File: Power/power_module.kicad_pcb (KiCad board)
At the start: 4 copper layers, 183 x 90 mm, 53 parts, among them J1 Conn_02x03_Odd_Even, J2 Conn_02x03_Odd_Even, J3 Conn_02x06_Counter_Clockwise, J4 Conn_02x05_Top_Bottom, J5 Conn_02x05_Top_Bottom, J6 Conn_02x02_Odd_Even, J7 Conn_02x02_Odd_Even, P3 CONN_01X04, P6 CONN_01X04, Q1 Q_NMOS_GDS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

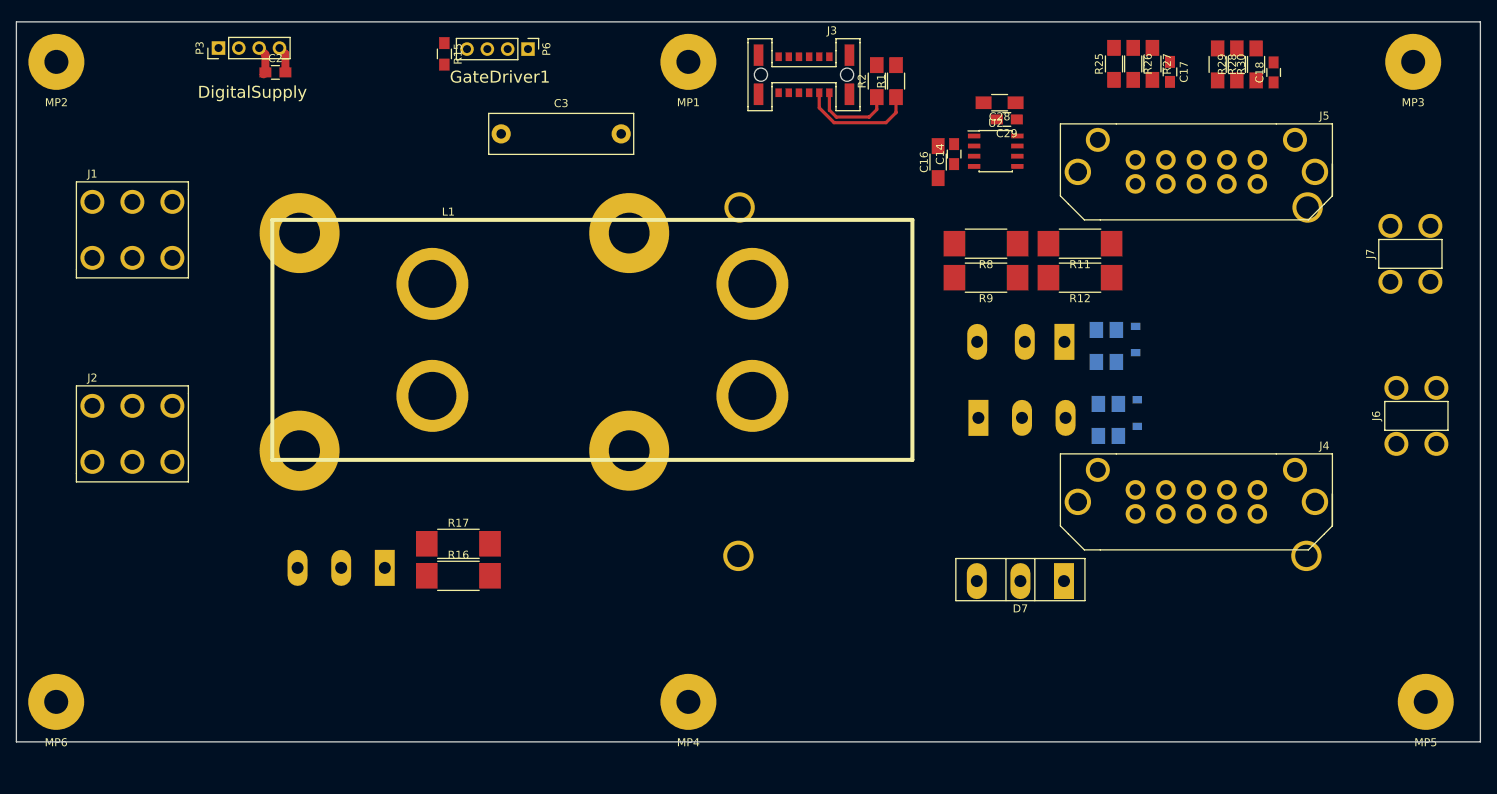
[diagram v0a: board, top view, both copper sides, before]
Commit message: Mevcut yerlesime gore kaba cizim yapildi.
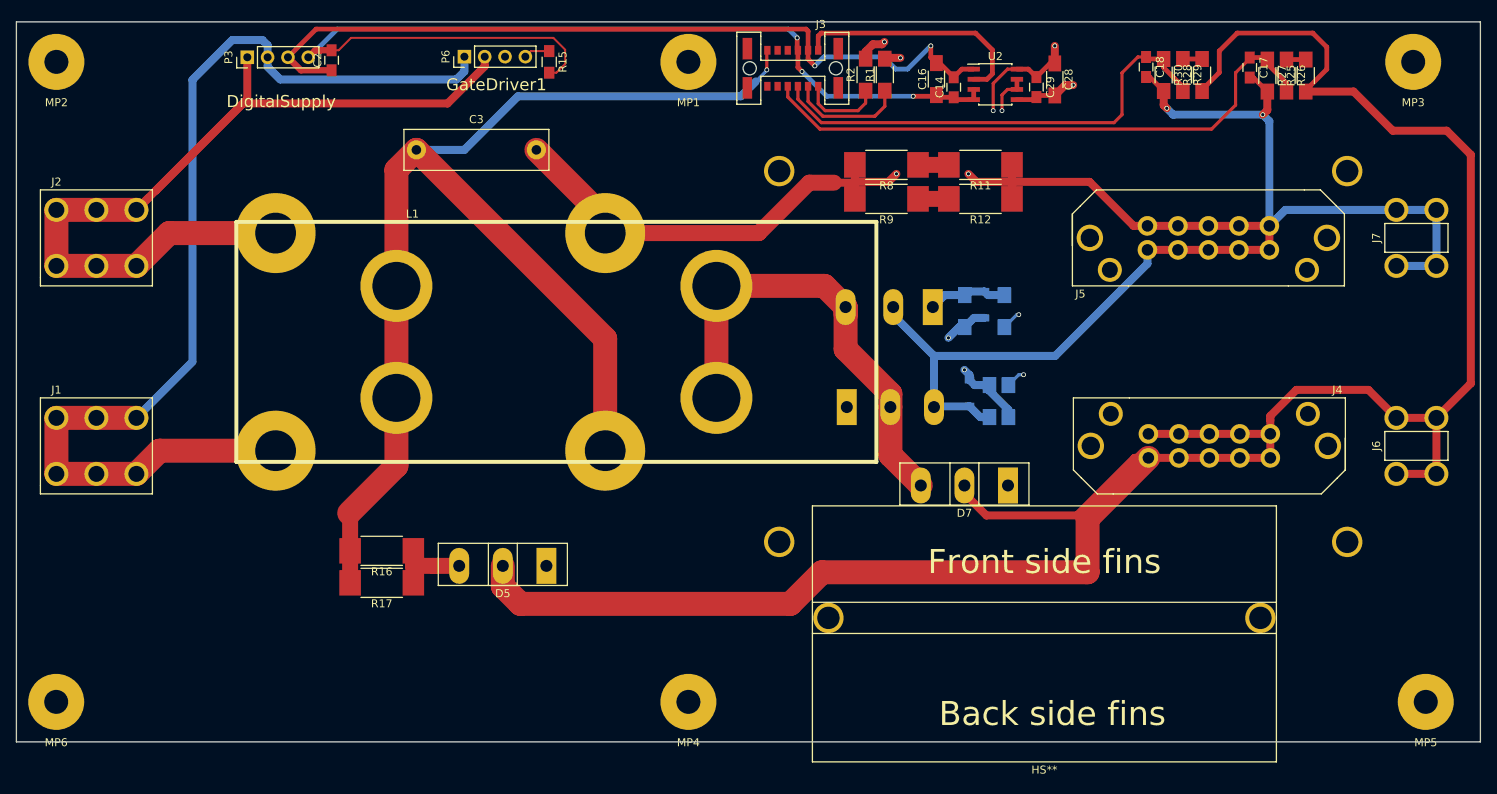
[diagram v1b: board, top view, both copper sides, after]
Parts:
- added HS**: HS_OhmiteC40, NamchoLibs:HS_OhmiteC40, F.Cu at (185.5, 149.5)
- D5: moved to F.Cu
- moved J1 27.4 mm to (67.0, 128.0)
- moved J2 24.9 mm to (67.0, 102.0)
- moved R25 24.0 mm to (218.2, 81.7)
- moved D3 21.1 mm to (176.1, 121.4), turned to 270 degrees
- moved D5 20.2 mm to (123.2, 143.0)
- moved D2 19.4 mm to (178.0, 110.3)
- moved R26 19.2 mm to (215.8, 81.7)
- moved Q1 17.0 mm to (171.6, 110.7)
- moved R31 17.0 mm to (175.6, 111.2)
- moved Q2 16.5 mm to (160.8, 123.2)
- moved R32 16.3 mm to (178.6, 122.4), turned to 90 degrees
- moved C18 16.0 mm to (198.2, 80.6), turned to 270 degrees
- moved R11 15.9 mm to (177.5, 92.9)
- moved R12 15.9 mm to (177.5, 97.1)
- moved R8 15.9 mm to (165.8, 92.9)
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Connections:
- D5 pad 2: Net-(D5-Pad2) -> /Vout+
- P6 pad 1: /PH2 -> /PH1
- P6 pad 2: /PH1 -> /PH2
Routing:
- net GNDA: track 0.15 -> 350.8 mm, vias 0 -> 7
- net /Vout+: track 0.00 -> 281.3 mm
- net Vin_Sens: track 0.00 -> 160.9 mm, vias 0 -> 1
- net /PH1: track 0.00 -> 132.7 mm
- net GNDD: track 3.46 -> 129.8 mm, vias 0 -> 3
- net /PH2: track 0.00 -> 121.8 mm
- net VDD: track 3.71 -> 102.5 mm, vias 0 -> 2
- net /15V/1: track 0.00 -> 88.7 mm, vias 0 -> 1
- net /Bridge-: track 0.00 -> 80.0 mm, vias 0 -> 2
- net Vout: track 0.00 -> 74.2 mm
- net Vop: track 0.00 -> 60.1 mm
- net /CrtPad: track 0.00 -> 58.4 mm
- net Net-(R14-Pad2): track 0.00 -> 44.4 mm, vias 0 -> 3
- net Gate_Drv: track 0.00 -> 30.2 mm
- net Net-(D3-Pad1): track 0.00 -> 26.5 mm, vias 0 -> 1
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
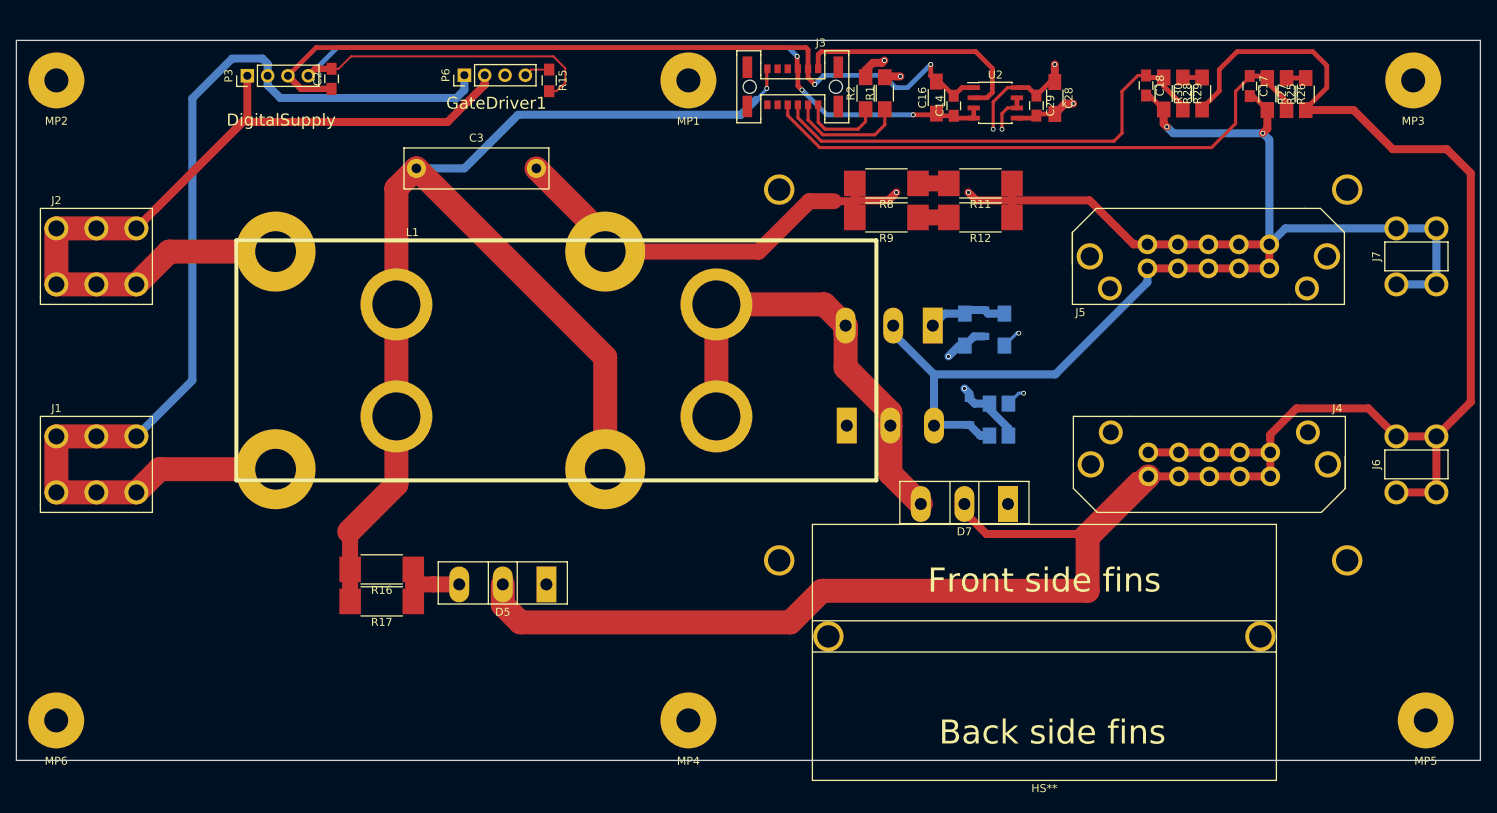
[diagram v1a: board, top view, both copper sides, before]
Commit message: Guc akisindaki hat/poligonlar tamamlandi.
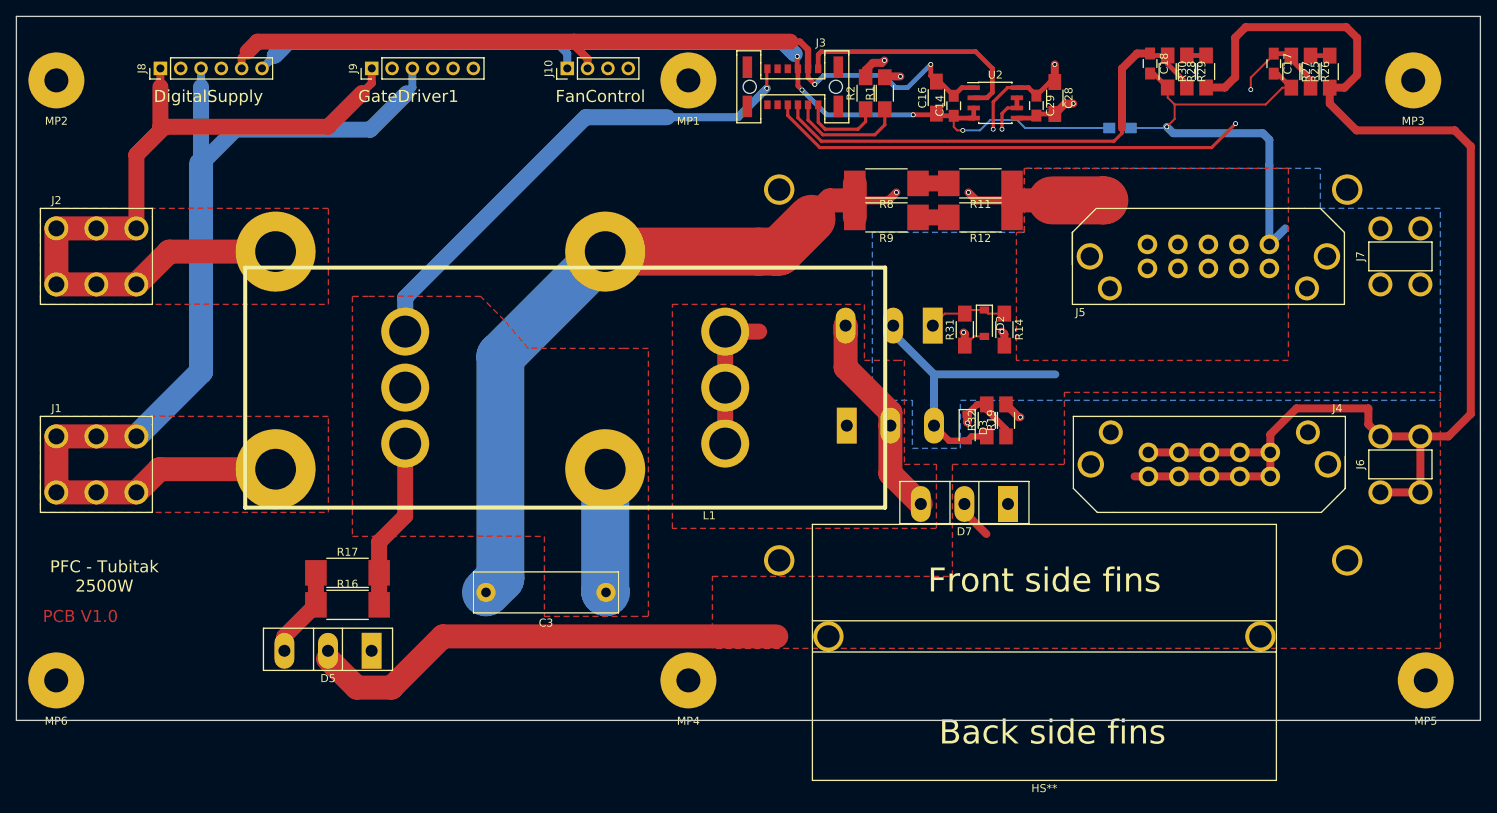
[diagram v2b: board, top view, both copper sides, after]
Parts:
- removed C2: 100n, Capacitors_SMD:C_0805_HandSoldering
- removed P3, P6: CONN_01X04, Pin_Headers:Pin_Header_Straight_1x04_Pitch2.54mm
- added J10: Conn_01x04, Pin_Headers:Pin_Header_Straight_1x04_Pitch2.54mm, F.Cu at (125.9, 78.5)
- added J8: Conn_01x06, Pin_Headers:Pin_Header_Straight_1x06_Pitch2.54mm, F.Cu at (75.0, 78.5)
- added J9: Conn_01x06, Pin_Headers:Pin_Header_Straight_1x06_Pitch2.54mm, F.Cu at (101.4, 78.5)
- D2, D3, R14, R19, R31, R32: moved to F.Cu
- L1: value INDUCTOR_2 -> INDUCTOR
- R15: moved to B.Cu
- moved R15 71.6 mm to (194.9, 86.0), turned to 180 degrees
- moved C3 58.1 mm to (130.7, 144.0), turned to 180 degrees
- moved D5 23.4 mm to (101.4, 151.3)
- moved R16 6.16 mm to (98.4, 145.6), turned to 0 degrees
- moved R17 5.56 mm to (98.4, 141.6), turned to 0 degrees
- moved MP4 5.00 mm to (141.0, 155.0)
- moved MP5 5.00 mm to (233.2, 155.0)
- moved MP6 5.00 mm to (62.0, 155.0)
- moved C17 4.10 mm to (214.2, 77.9)
- moved R25 4.10 mm to (221.2, 78.9)
- moved R26 4.10 mm to (218.8, 78.9)
- moved R27 4.10 mm to (216.4, 78.9)
- moved L1 3.57 mm to (125.6, 118.4), turned to 180 degrees
- moved C18 2.80 mm to (198.7, 77.9)
- moved R28 2.80 mm to (205.7, 78.9)
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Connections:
- J3 pad 4: Net-(J3-Pad4) -> (no net)
- J3 pad 5: Net-(J3-Pad5) -> (no net)
- J3 pad 7: Net-(J3-Pad7) -> (no net)
- J3 pad 8: Net-(J3-Pad8) -> (no net)
- L1 pad 1: Vin_Sens -> /CrtPad
- MP1 pad 1: Net-(MP1-Pad1) -> (no net)
- MP2 pad 1: Net-(MP2-Pad1) -> (no net)
- MP3 pad 1: Net-(MP3-Pad1) -> (no net)
- MP4 pad 1: Net-(MP4-Pad1) -> (no net)
- MP5 pad 1: Net-(MP5-Pad1) -> (no net)
- MP6 pad 1: Net-(MP6-Pad1) -> (no net)
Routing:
- net Vin_Sens: track 160.9 -> 105.3 mm
- net GNDA: track 350.8 -> 300.2 mm, vias 7 -> 6
- net /Vout+: track 281.3 -> 235.5 mm
- net /Bridge-: track 80.0 -> 116.7 mm
- net Net-(R14-Pad2): track 44.4 -> 70.4 mm
- net /15V/1: track 88.7 -> 101.8 mm
- net /CrtPad: track 58.4 -> 45.4 mm
- net Vop: track 60.1 -> 66.9 mm
- net /PH1: track 132.7 -> 127.8 mm
- net VDD: track 102.5 -> 107.2 mm
- net Vout: track 74.2 -> 78.2 mm, vias 0 -> 2
- net GNDD: track 129.8 -> 126.2 mm, vias 3 -> 4
- net /PH2: track 121.8 -> 123.8 mm
- net Net-(D3-Pad1): track 26.5 -> 28.5 mm
- net Net-(D5-Pad3): track 9.73 -> 11.4 mm
- added copper zone on F.Cu, net /CrtPad
- added copper zone on F.Cu, net /PH1
- added copper zone on F.Cu, net /PH2
- added copper zone on F.Cu, net /Vout+
- added copper zone on B.Cu, net GNDA
- added copper zone on F.Cu, net GNDA
- added copper zone on In2.Cu, net GNDA
- added copper zone on F.Cu, net Vin_Sens
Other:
- board size 183 x 90 mm -> 183 x 88 mm
- board text added: "FanControl"
- board text added: "PCB V1.0"
- board text added: "PFC - Tubitak 2500W"

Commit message: Poligon eklemeleri yapildi. Hatlar iyilestirildi.
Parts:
- turned R19 to 270 degrees
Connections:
- net Net-(D2-Pad1) renamed /Gate1
- net Net-(D3-Pad1) renamed /Gate2
- net Net-(R14-Pad2) renamed /Drv_Out
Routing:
- net GNDA: track 300.2 -> 244.8 mm, vias 6 -> 7
- net /Drv_Out: track 70.4 -> 43.4 mm
- net /PH2: track 123.8 -> 102.9 mm
- net /15V/1: track 101.8 -> 93.1 mm
- net /Vout+: track 235.5 -> 227.8 mm, vias 0 -> 2
- net Vout: track 78.2 -> 81.4 mm, vias 2 -> 0
- net /Gate2: track 28.5 -> 26.3 mm
- net VDD: track 107.2 -> 105.9 mm, vias 2 -> 3
- net GNDD: track 126.2 -> 127.0 mm
- added copper zone on F.Cu, net /Bridge-
- added copper zone on In1.Cu, net /Drv_Out
- added copper zone on F.Cu, net /Gate1
- added copper zone on F.Cu, net /Gate2
- added copper zone on In1.Cu, net /Gate2
- added copper zone on In1.Cu, net GNDA

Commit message: Kontrol karti semasi cizildi. Layout yerlestirme yapildi.
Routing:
- net GNDA: track 244.8 -> 208.2 mm, vias 7 -> 10
- net /Drv_Out: track 43.4 -> 9.22 mm, vias 3 -> 4
- net /CrtPad: track 45.4 -> 18.2 mm
- net Vin_Sens: track 105.3 -> 89.9 mm
- net /Bridge-: track 116.7 -> 120.6 mm
- net VDD: track 105.9 -> 108.9 mm, vias 3 -> 2
- net /Gate2: track 26.3 -> 23.8 mm, vias 1 -> 4
- net /Gate1: track 9.94 -> 9.31 mm
- added copper zone on B.Cu, net Vin_Sens
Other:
- board text added: "Bottom Layer"
- board text added: "In Layer-1"
- board text added: "In Layer-2"
- board text added: "Top layer"

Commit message: Güc kartina EMI filtresi eklendi. Güc kartindaki mosfet driver + ve - ile beslenebilecek sekilde duzenlendi. Güc ve kontrol kartlari icin BOM uretildi.
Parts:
- removed C29: 10n, Capacitors_SMD:C_0805_HandSoldering
- removed R15: R_Small, Resistors_SMD:R_0805_HandSoldering
- added C1: 1u, Capacitors_SMD:C_1206_HandSoldering, F.Cu at (244.8, 79.6)
- added C2: C, Capacitors_ThroughHole:CP_Axial_L30.0mm_D10.0mm_P35.00mm_Horizontal, F.Cu at (77.7, 95.3)
- added C4: C, Capacitors_ThroughHole:CP_Axial_L30.0mm_D10.0mm_P35.00mm_Horizontal, F.Cu at (133.8, 95.8)
- added C5: 100n, Capacitors_ThroughHole:C_Rect_L18.0mm_W8.0mm_P15.00mm_FKS3_FKP3, F.Cu at (98.0, 80.0)
- added C6: 100n, Capacitors_ThroughHole:C_Rect_L18.0mm_W8.0mm_P15.00mm_FKS3_FKP3, F.Cu at (113.0, 146.0)
- added FL1: EMI_Filter_CommonMode, NamchoLibs:RB6522_Size4, F.Cu at (105.2, 112.9)
- added J11: Conn_02x02_Odd_Even, NamchoLibs:Conn_4pins_15A, F.Cu at (60.0, 145.0)
- added R3: R_Small, Resistors_SMD:R_0805_HandSoldering, F.Cu at (242.6, 79.6)
- moved C28 60.4 mm to (247.2, 79.6), turned to 90 degrees
- moved MP3 58.0 mm to (289.6, 77.6)
- moved MP5 58.0 mm to (291.2, 152.6)
- moved R26 58.0 mm to (276.8, 76.5)
- moved J10 58.0 mm to (183.9, 76.1)
- moved R16 58.0 mm to (156.4, 143.2)
- moved R17 58.0 mm to (156.4, 139.2)
- moved C14 58.0 mm to (232.2, 80.8)
- moved C16 58.0 mm to (230.0, 79.8)
- moved C17 58.0 mm to (272.2, 75.5)
- moved C18 58.0 mm to (256.7, 75.5)
- moved C3 58.0 mm to (188.7, 141.6)
- moved D1 58.0 mm to (168.0, 112.6)
- moved D2 58.0 mm to (236.0, 108.0)
- moved D3 58.0 mm to (233.8, 121.0)
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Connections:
- C14 pad 1: GNDD -> GNDA
- C16 pad 1: GNDD -> GNDA
- C28 pad 1: GNDA -> /15V/1
- C28 pad 2: /15V/1 -> GNDA
- D1 pad 2: /PH2 -> /PH1
- D1 pad 4: /PH1 -> /PH2
- J1 pad 1: /PH1 -> /Line2
- J1 pad 2: /PH1 -> /Line2
- J1 pad 3: /PH1 -> /Line2
- J1 pad 4: /PH1 -> /Line2
- J1 pad 5: /PH1 -> /Line2
- J1 pad 6: /PH1 -> /Line2
- J10 pad 1: GNDD -> GNDA
- J2 pad 1: /PH2 -> /Line1
- J2 pad 2: /PH2 -> /Line1
- J2 pad 3: /PH2 -> /Line1
- J2 pad 4: /PH2 -> /Line1
- J2 pad 5: /PH2 -> /Line1
- J2 pad 6: /PH2 -> /Line1
- J3 pad 3: GNDD -> GNDA
- J8 pad 1: /PH2 -> /PH1
- J8 pad 3: /PH1 -> /PH2
- J8 pad 6: GNDD -> GNDA
- J9 pad 1: /PH2 -> /PH1
- J9 pad 3: /PH1 -> /PH2
- J9 pad 6: GNDA -> /GND_DRV1
- MP6 pad 1: (no net) -> Earth
- U2 pad 3: GNDD -> GNDA
- U2 pad 4: GNDD -> GNDA
- U2 pad 8: GNDA -> /GND_DRV1
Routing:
- net GNDD: track 127.0 -> 0.00 mm, vias 4 -> 0
- net /GND_DRV1: track 0.00 -> 92.5 mm, vias 0 -> 3
- net Earth: track 0.00 -> 76.7 mm
- net /PH1: track 127.8 -> 71.6 mm
- net GNDA: track 208.2 -> 237.5 mm, vias 10 -> 11
- net VDD: track 108.9 -> 95.1 mm, vias 2 -> 6
- net /Vout+: track 227.8 -> 221.9 mm
- net /15V/1: track 93.1 -> 98.1 mm
- net /Gate2: track 23.8 -> 26.0 mm
- net /Drv_Out: track 9.22 -> 7.41 mm, vias 4 -> 5
- net /PH2: track 102.9 -> 101.5 mm
- added copper zone on F.Cu, net /Drv_Out
- added copper zone on F.Cu, net /GND_DRV1
- added copper zone on F.Cu, net /Line1
- added copper zone on F.Cu, net /Line2
- added copper zone on B.Cu, net /PH2
- added copper zone on F.Cu, net Earth
- added copper zone on F.Cu, net VDD
- added copper zone on In2.Cu, net VDD
- removed copper zone on F.Cu, net /PH2
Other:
- board size 183 x 88 mm -> 248 x 88 mm
- board text added: "+15V"
- board text added: "GNDD"
- board text added: "GND_DRV"
- board text added: "Line1"
- board text added: "Line2"
- board text added: "VDD"

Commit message: Hatali Mosfet paketi duzeltildi. EMI filtre kaldirildi ve kart boyu kisaldi. TO247-2 paketli boost diyodu kullanildi.
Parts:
- removed C2, C4: C, Capacitors_ThroughHole:CP_Axial_L30.0mm_D10.0mm_P35.00mm_Horizontal
- removed D7: C5D50065D, TO_SOT_Packages_THT:TO-247_TO-3P_Vertical
- removed FL1: EMI_Filter_CommonMode, NamchoLibs:RB6522_Size4
- removed HS** (x2): HS_OhmiteB60C60, NamchoLibs:HS_OhmiteB60C60
- removed HS**: HS_OhmiteC40, NamchoLibs:HS_OhmiteC40
- added D4: C4D20120H, TO_SOT_Packages_THT:TO-247-2_Vertical, B.Cu at (231.0, 131.9)
- moved C5 79.0 mm to (127.8, 153.2), turned to 90 degrees
- moved J11 50.2 mm to (110.0, 140.0)
- moved J2 50.2 mm to (110.0, 95.0)
- moved J1 50.2 mm to (110.0, 121.8)
- moved C6 25.1 mm to (136.9, 138.2), turned to 270 degrees
- moved MP2 20.0 mm to (110.0, 77.6)
- moved MP6 20.0 mm to (110.0, 152.6)
- moved Q2 17.6 mm to (234.6, 113.0)
- moved D3 15.6 mm to (240.1, 106.7), turned to 0 degrees
- moved D2 14.6 mm to (221.4, 106.8), turned to 0 degrees
- moved R19 14.6 mm to (232.8, 106.7), turned to 90 degrees
- moved Q1 14.4 mm to (216.0, 113.0), turned to 0 degrees
- moved R32 13.4 mm to (235.2, 106.7), turned to 270 degrees
- moved R14 10.2 mm to (228.5, 106.8)
- moved R31 7.70 mm to (226.1, 106.8)
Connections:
- C5 pad 2: /PH1 -> /Line1
- C6 pad 1: /PH2 -> /Line2
- D1 pad 2: /PH1 -> /Line1
- D1 pad 4: /PH2 -> /Line2
- J10 pad 3: (no net) -> /FAN2
- J10 pad 4: (no net) -> /FAN1
- J3 pad 4: (no net) -> Net-(J3-Pad4)
- J3 pad 5: (no net) -> Net-(J3-Pad5)
- J3 pad 7: (no net) -> Net-(J3-Pad7)
- J3 pad 8: (no net) -> Net-(J3-Pad8)
- J8 pad 1: /PH1 -> /Line1
- J8 pad 2: (no net) -> Net-(J8-Pad2)
- J8 pad 3: /PH2 -> /Line2
- J8 pad 4: (no net) -> Net-(J8-Pad4)
- J9 pad 1: /PH1 -> /Line1
- J9 pad 2: (no net) -> Net-(J9-Pad2)
- J9 pad 3: /PH2 -> /Line2
- J9 pad 4: (no net) -> Net-(J9-Pad4)
- MP1 pad 1: (no net) -> Net-(MP1-Pad1)
- MP2 pad 1: (no net) -> Net-(MP2-Pad1)
- MP3 pad 1: (no net) -> Net-(MP3-Pad1)
- MP4 pad 1: (no net) -> Net-(MP4-Pad1)
- MP5 pad 1: (no net) -> Net-(MP5-Pad1)
- Q1 pad 2: GNDA -> /CrtPad
- Q1 pad 3: /CrtPad -> GNDA
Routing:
- net /Line1: track 0.00 -> 176.6 mm
- net /Line2: track 0.00 -> 154.8 mm
- net /PH2: track 101.5 -> 0.00 mm
- net /PH1: track 71.6 -> 0.00 mm
- net Earth: track 76.7 -> 54.3 mm
- net /Gate2: track 26.0 -> 11.3 mm, vias 4 -> 0
- net GNDA: track 237.5 -> 227.4 mm, vias 11 -> 10
- net /Drv_Out: track 7.41 -> 14.8 mm, vias 5 -> 15
- net /Vout+: track 221.9 -> 217.0 mm
- net /Gate1: track 9.31 -> 12.0 mm, vias 0 -> 1
- net (no net): vias 0 -> 5
- added copper zone on In1.Cu, net /Gate1
- added copper zone on B.Cu, net /Line2
- removed copper zone on In1.Cu, net /Gate2
- removed copper zone on F.Cu, net /Line2
- removed copper zone on F.Cu, net /PH1
- removed copper zone on B.Cu, net /PH2
- removed copper zone on In1.Cu, net GNDA
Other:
- board size 248 x 88 mm -> 198 x 88 mm
